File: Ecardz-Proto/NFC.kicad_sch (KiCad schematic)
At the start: 1 part, among them J1 Raspberry_Pi_2_3

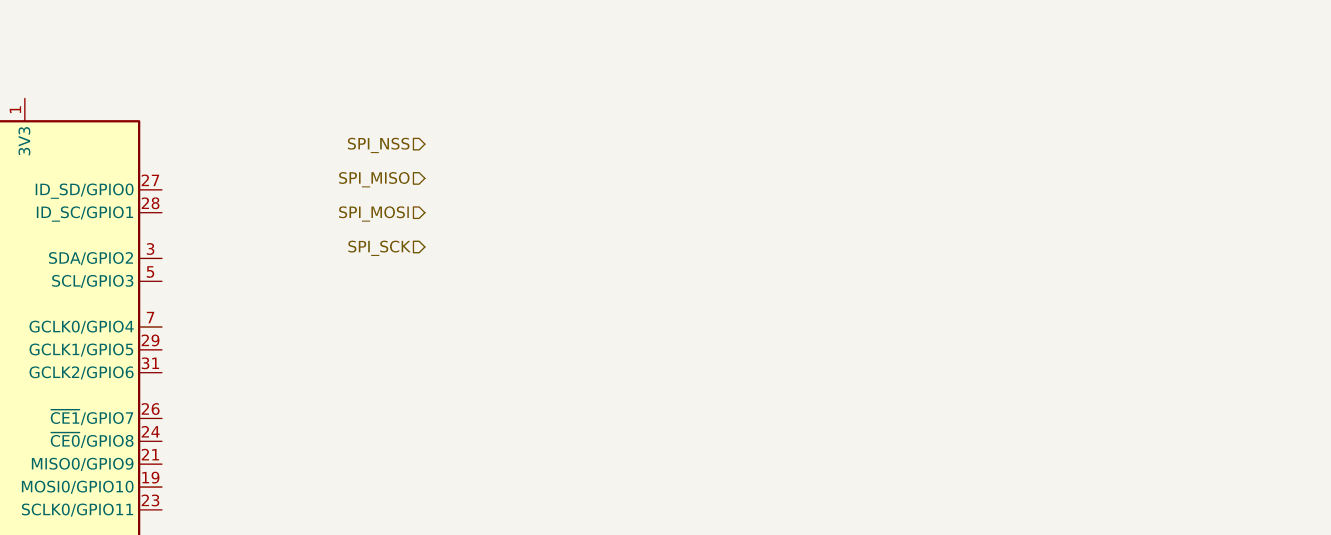
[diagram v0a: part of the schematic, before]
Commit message: added energy harvesting sensing ADC to NFC
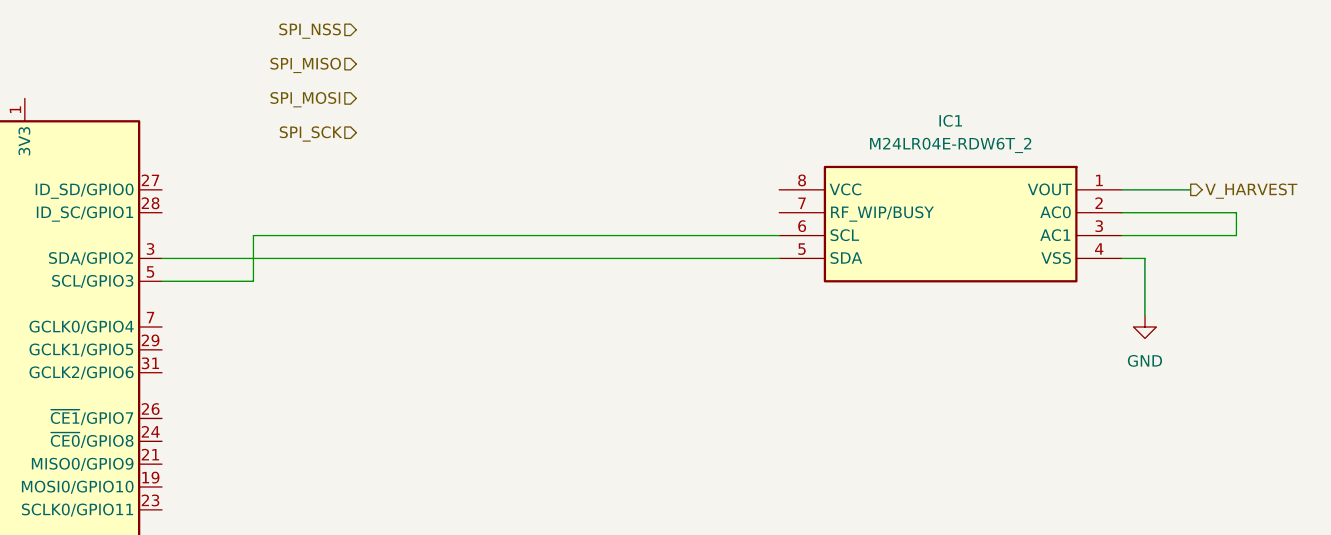
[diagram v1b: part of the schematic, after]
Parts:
- added IC1: M24LR04E-RDW6T_2, SOP65P640X120-8N, symbol SamacSys_Parts:M24LR04E-RDW6T_2
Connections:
- net at J1.3 (SDA/GPIO2): now also IC1.5 (SDA)
- net at J1.5 (SCL/GPIO3): now also IC1.6 (SCL)
- new net: IC1.2 (AC0), IC1.3 (AC1)
- new net GND: IC1.4 (VSS)
- new net V_HARVEST: IC1.1 (VOUT)

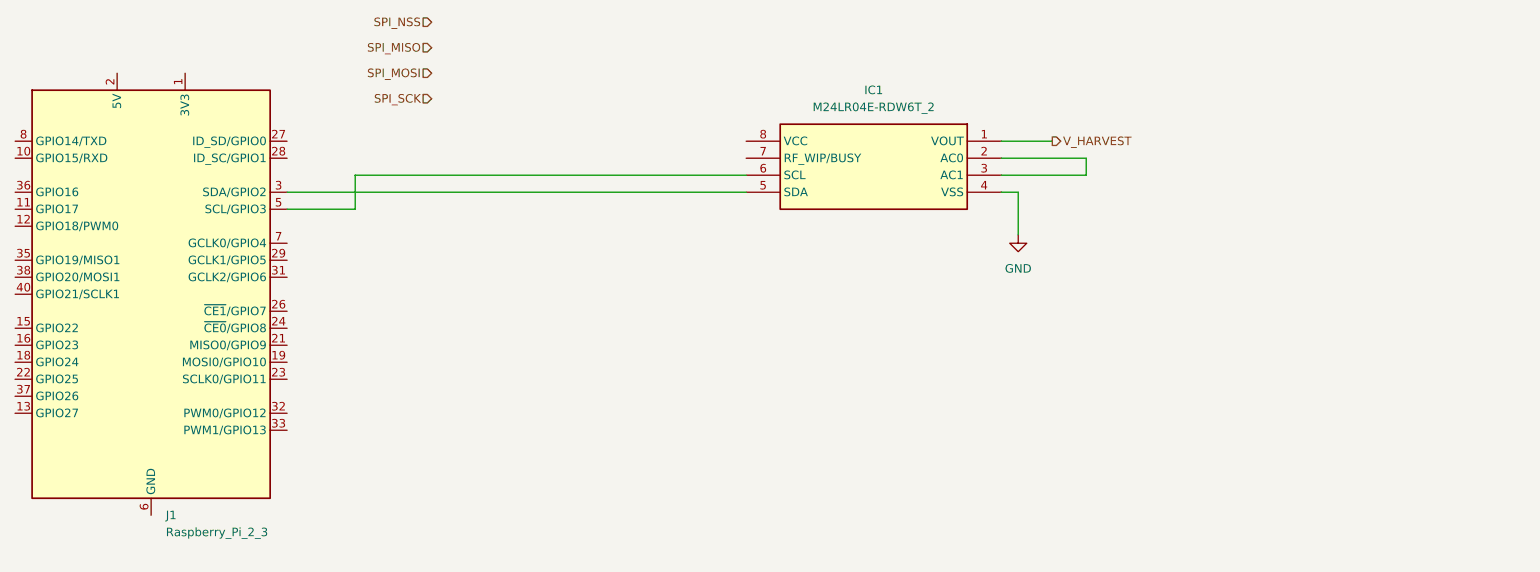
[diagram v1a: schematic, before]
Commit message: added STM and rpi pin connections.
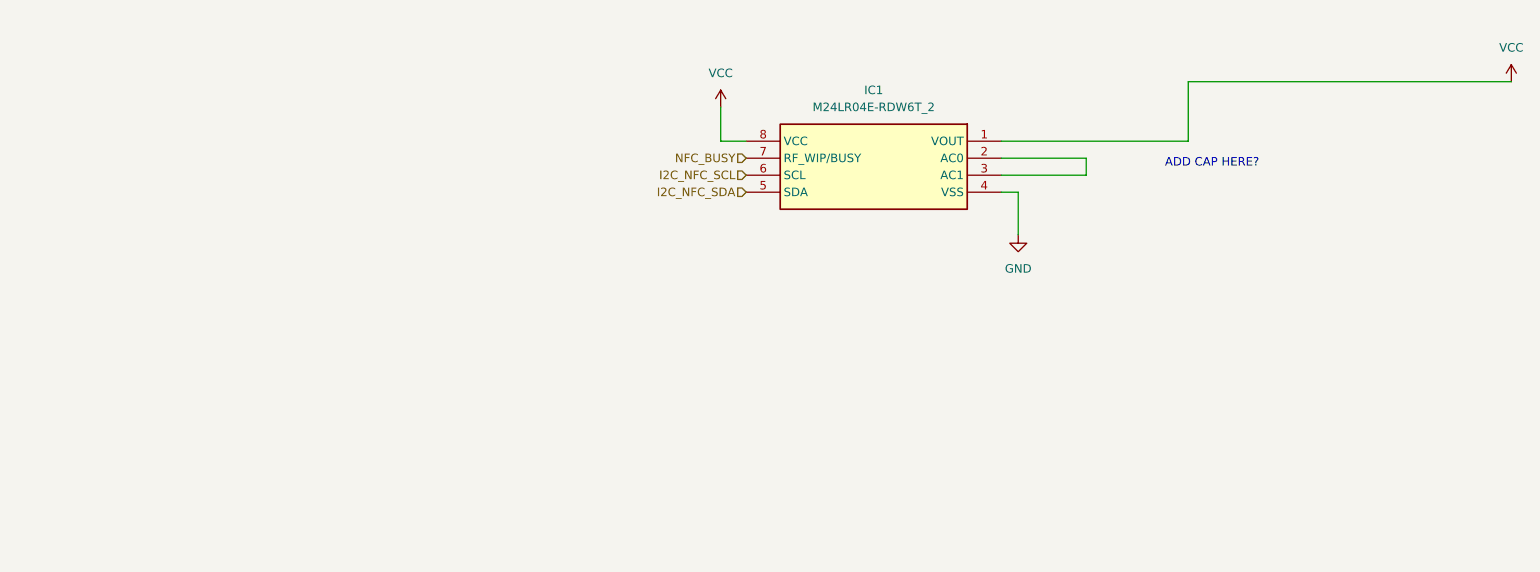
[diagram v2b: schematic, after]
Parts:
- removed J1: Raspberry_Pi_2_3, symbol Connector:Raspberry_Pi_2_3
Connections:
- net V_HARVEST is gone; now on net VCC: IC1.1 (VOUT)
- net I2C_NFC_SDA: now reaches IC1.5 (SDA)
- net I2C_NFC_SCL: now reaches IC1.6 (SCL)
- net NFC_BUSY: now reaches IC1.7 (RF_WIP/BUSY)
- net VCC: now reaches IC1.8 (VCC)
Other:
- note added: "ADD CAP HERE?"
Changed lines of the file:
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@@
 	(wire
 		(pts
-			(xy 81.28 39.37) (xy 81.28 44.45)
-		)
-		(stroke
-			(width 0)
-			(type default)
-		)
-	)
-	(wire
-		(pts
-			(xy 139.7 39.37) (xy 81.28 39.37)
+			(xy 135.89 34.29) (xy 139.7 34.29)
 		)
 		(stroke
@@
 	(wire
 		(pts
+			(xy 205.74 34.29) (xy 177.8 34.29)
+		)
+		(stroke
+			(width 0)
+			(type default)
+		)
+	)
+	(wire
+		(pts
 			(xy 177.8 36.83) (xy 190.5 36.83)
 		)
@@
 	(wire
 		(pts
-			(xy 177.8 34.29) (xy 185.42 34.29)
+			(xy 135.89 29.21) (xy 135.89 34.29)
+		)
+		(stroke
+			(width 0)
+			(type default)
+		)
+	)
+	(wire
+		(pts
+			(xy 205.74 25.4) (xy 254 25.4)
 		)
 		(stroke
@@
 	(wire
 		(pts
-			(xy 81.28 44.45) (xy 71.12 44.45)
-		)
-		(stroke
-			(width 0)
-			(type default)
-		)
-	)
-	(wire
-		(pts
 			(xy 180.34 48.26) (xy 180.34 41.91)
 		)
@@
 	(wire
 		(pts
-			(xy 71.12 41.91) (xy 139.7 41.91)
-		)
-		(stroke
-			(width 0)
-			(type default)
-		)
-	)
-	(hierarchical_label "SPI_MISO"
-		(shape input)
-		(at 92.71 20.32 180)
-		(fields_autoplaced yes)
+			(xy 205.74 25.4) (xy 205.74 34.29)
+		)
+		(stroke
+			(width 0)
+			(type default)
+		)
+	)
+	(text "ADD CAP HERE?\n"
+		(exclude_from_sim no)
+		(at 209.296 37.592 0)
 		(effects
 			(font
 				(size 1.27 1.27)
 			)
-			(justify right)
-		)
-	)
-	(hierarchical_label "SPI_MOSI"
+		)
+	)
+	(hierarchical_label "I2C_NFC_SDA"
 		(shape input)
-		(at 92.71 24.13 180)
+		(at 139.7 41.91 180)
 		(fields_autoplaced yes)
 		(effects
@@
 		)
 	)
-	(hierarchical_label "V_HARVEST"
-		(shape output)
-		(at 185.42 34.29 0)
+	(hierarchical_label "NFC_BUSY"
+		(shape input)
+		(at 139.7 36.83 180)
 		(fields_autoplaced yes)
 		(effects
@@
 				(size 1.27 1.27)
 			)
-			(justify left)
-		)
-	)
-	(hierarchical_label "SPI_SCK"
+			(justify right)
+		)
+	)
+	(hierarchical_label "I2C_NFC_SCL"
 		(shape input)
-		(at 92.71 27.94 180)
+		(at 139.7 39.37 180)
 		(fields_autoplaced yes)
 		(effects
@@
 		)
 	)
-	(hierarchical_label "SPI_NSS"
-		(shape input)
-		(at 92.71 16.51 180)
-		(fields_autoplaced yes)
-		(effects
-			(font
-				(size 1.27 1.27)
-			)
-			(justify right)
+	(symbol
+		(lib_id "power:VCC")
+		(at 135.89 29.21 0)
+		(unit 1)
+		(exclude_from_sim no)
+		(in_bom yes)
+		(on_board yes)
+		(dnp no)
+		(fields_autoplaced yes)
+		(property "Reference" "#PWR011"
+			(at 135.89 33.02 0)
+			(effects
+				(font
+					(size 1.27 1.27)
+				)
+				(hide yes)
+			)
+		)
+		(property "Value" "VCC"
+			(at 135.89 24.13 0)
+			(effects
+				(font
+					(size 1.27 1.27)
+				)
+			)
+		)
+		(property "Footprint" ""
+			(at 135.89 29.21 0)
+			(effects
+				(font
+					(size 1.27 1.27)
+				)
+				(hide yes)
+			)
+		)
+		(property "Datasheet" ""
+			(at 135.89 29.21 0)
+			(effects
+				(font
+					(size 1.27 1.27)
+				)
+				(hide yes)
+			)
+		)
+		(property "Description" "Power symbol creates a global label with name \"VCC\""
+			(at 135.89 29.21 0)
+			(effects
+				(font
+					(size 1.27 1.27)
+				)
+				(hide yes)
+			)
+		)
+		(pin "1"
+		)
+		(instances
+			(project "Ecardz-Proto"
+				(path "/2adbba85-9270-4efb-857d-656bb51406ca/95527a5c-8cb7-439d-944b-2d67c4df2ece"
+					(reference "#PWR011")
+					(unit 1)
+				)
+			)
 		)
 	)
@@
 		)
 		(instances
-			(project ""
+			(project "Ecardz-Proto"
 				(path "/2adbba85-9270-4efb-857d-656bb51406ca/95527a5c-8cb7-439d-944b-2d67c4df2ece"
 					(reference "IC1")
@@
 		)
 		(instances
-			(project ""
+			(project "Ecardz-Proto"
 				(path "/2adbba85-9270-4efb-857d-656bb51406ca/95527a5c-8cb7-439d-944b-2d67c4df2ece"
 					(reference "#PWR06")
@@
 	)
 	(symbol
-		(lib_id "Connector:Raspberry_Pi_2_3")
-		(at 50.8 57.15 0)
+		(lib_id "power:VCC")
+		(at 254 25.4 0)
 		(unit 1)
 		(exclude_from_sim no)
@@
 		(dnp no)
 		(fields_autoplaced yes)
-		(property "Reference" "J1"
-			(at 52.9941 90.17 0)
-			(effects
-				(font
-					(size 1.27 1.27)
-				)
-				(justify left)
-			)
-		)
-		(property "Value" "Raspberry_Pi_2_3"
-			(at 52.9941 92.71 0)
-			(effects
-				(font
-					(size 1.27 1.27)
-				)
-				(justify left)
+		(property "Reference" "#PWR010"
+			(at 254 29.21 0)
+			(effects
+				(font
+					(size 1.27 1.27)
+				)
+				(hide yes)
+			)
+		)
+		(property "Value" "VCC"
+			(at 254 20.32 0)
+			(effects
+				(font
+					(size 1.27 1.27)
+				)
 			)
 		)
 		(property "Footprint" ""
-			(at 50.8 57.15 0)
-			(effects
-				(font
-					(size 1.27 1.27)
-				)
-				(hide yes)
-			)
-		)
-		(property "Datasheet" "https://www.raspberrypi.org/documentation/hardware/raspberrypi/schematics/rpi_SCH_3bplus_1p0_reduced.pdf"
-			(at 111.76 101.6 0)
-			(effects
-				(font
-					(size 1.27 1.27)
-				)
-				(hide yes)
-			)
-		)
-		(property "Description" "expansion header for Raspberry Pi 2 & 3"
-			(at 50.8 57.15 0)
-			(effects
-				(font
-					(size 1.27 1.27)
-				)
-				(hide yes)
-			)
-		)
-		(pin "11"
-		)
-		(pin "19"
-		)
-		(pin "28"
-		)
-		(pin "30"
-		)
-		(pin "15"
-		)
-		(pin "20"
-		)
-		(pin "12"
-		)
-		(pin "17"
-		)
-		(pin "2"
-		)
-		(pin "25"
-		)
-		(pin "29"
-		)
-		(pin "13"
+			(at 254 25.4 0)
+			(effects
+				(font
+					(size 1.27 1.27)
+				)
+				(hide yes)
+			)
+		)
+		(property "Datasheet" ""
+			(at 254 25.4 0)
+			(effects
+				(font
+					(size 1.27 1.27)
+				)
+				(hide yes)
+			)
+		)
+		(property "Description" "Power symbol creates a global label with name \"VCC\""
+			(at 254 25.4 0)
+			(effects
+				(font
+					(size 1.27 1.27)
+				)
+				(hide yes)
+			)
 		)
 		(pin "1"
-		)
-		(pin "14"
-		)
-		(pin "16"
-		)
-		(pin "27"
-		)
-		(pin "33"
-		)
-		(pin "3"
-		)
-		(pin "26"
-		)
-		(pin "32"
-		)
-		(pin "36"
-		)
-		(pin "18"
-		)
-		(pin "24"
-		)
-		(pin "23"
-		)
-		(pin "39"
-		)
-		(pin "4"
-		)
-		(pin "40"
-		)
-		(pin "35"
-		)
-		(pin "6"
-		)
-		(pin "38"
-		)
-		(pin "7"
-		)
-		(pin "5"
-		)
-		(pin "37"
-		)
-		(pin "8"
-		)
-		(pin "9"
-		)
-		(pin "34"
-		)
-		(pin "21"
-		)
-		(pin "10"
-		)
-		(pin "31"
-		)
-		(pin "22"
 		)
 		(instances
 			(project "Ecardz-Proto"
 				(path "/2adbba85-9270-4efb-857d-656bb51406ca/95527a5c-8cb7-439d-944b-2d67c4df2ece"
-					(reference "J1")
+					(reference "#PWR010")
 					(unit 1)
 				)

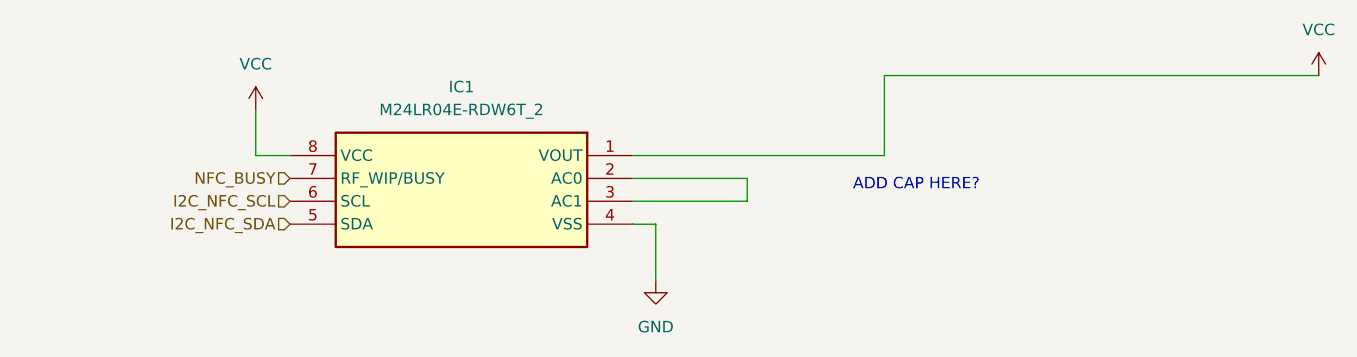
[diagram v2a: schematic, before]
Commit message: made all supply voltages VDD rather than mix of VDD/VCC, added VDD measurement via STM32 internal ADC, put DNP jumper for VPP on E-ink connector, and made NFC VCC pin only connected to power if externally powered
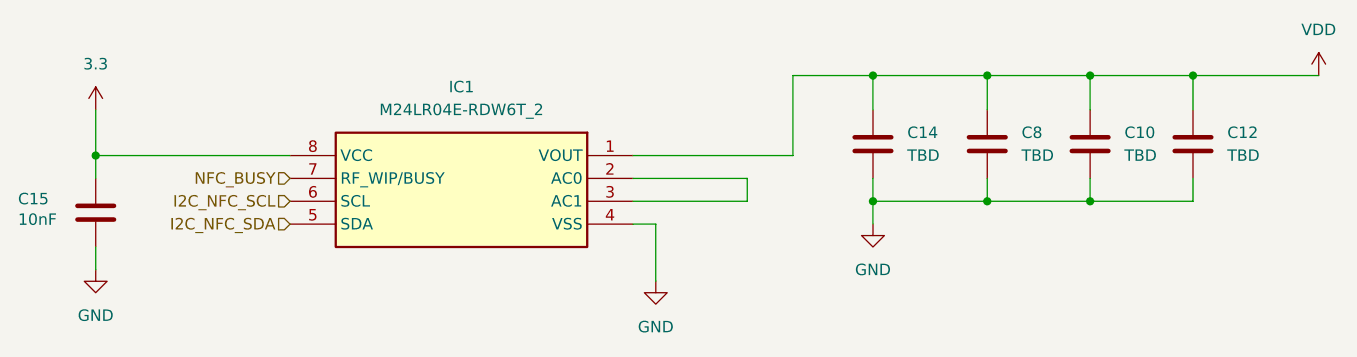
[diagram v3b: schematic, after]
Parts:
- added C10, C12, C14, C8: TBD, symbol Device:C
- added C15: 10nF, symbol Device:C
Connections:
- net GND: now also C10.2, C12.2, C14.2, C15.2, C8.2
- net VCC renamed 3.3
- net 3.3: now also C15.1; no longer IC1.1 (VOUT)
- new net VDD: C10.1, C12.1, C14.1, C8.1, IC1.1 (VOUT)
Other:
- note removed: "ADD CAP HERE?"

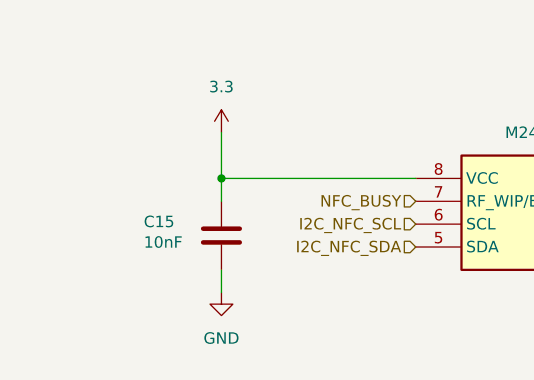
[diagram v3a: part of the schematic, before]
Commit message: added jumpers to select NFC chip's power supply connection
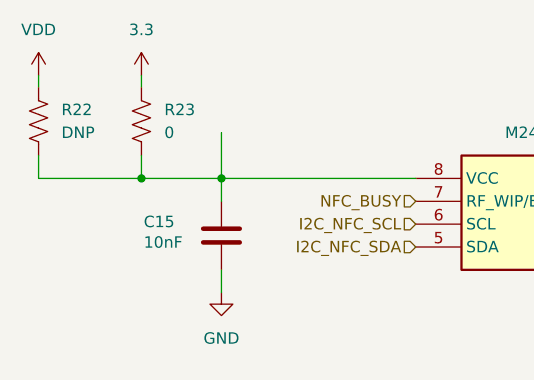
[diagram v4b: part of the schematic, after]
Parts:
- added R22: DNP, Resistor_SMD:R_0603_1608Metric_Pad0.98x0.95mm_HandSolder, symbol Device:R_US
- added R23: 0, Resistor_SMD:R_0603_1608Metric_Pad0.98x0.95mm_HandSolder, symbol Device:R_US
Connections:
- net 3.3: now also R23.2; no longer C15.1, IC1.8 (VCC)
- net VDD: now also R22.2
- new net: C15.1, IC1.8 (VCC), R22.1, R23.1

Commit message: updated most footprints
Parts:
- C10, C12, C14, C15, C8: footprint (none) -> Capacitor_SMD:C_0603_1608Metric_Pad1.08x0.95mm_HandSolder
- R23: value 0 -> DNP
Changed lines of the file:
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@@
 	(wire
 		(pts
-			(xy 118.11 29.21) (xy 118.11 34.29)
+			(xy 97.79 22.86) (xy 97.79 24.13)
 		)
 		(stroke
@@
 	(wire
 		(pts
-			(xy 97.79 22.86) (xy 97.79 24.13)
+			(xy 228.6 39.37) (xy 240.03 39.37)
 		)
 		(stroke
@@
 	(wire
 		(pts
-			(xy 228.6 39.37) (xy 240.03 39.37)
+			(xy 195.58 25.4) (xy 204.47 25.4)
 		)
 		(stroke
@@
 	(wire
 		(pts
-			(xy 195.58 25.4) (xy 204.47 25.4)
+			(xy 204.47 36.83) (xy 204.47 39.37)
 		)
 		(stroke
@@
 	(wire
 		(pts
-			(xy 204.47 36.83) (xy 204.47 39.37)
+			(xy 190.5 36.83) (xy 190.5 39.37)
 		)
 		(stroke
@@
 	(wire
 		(pts
-			(xy 190.5 36.83) (xy 190.5 39.37)
+			(xy 240.03 39.37) (xy 240.03 36.83)
 		)
 		(stroke
@@
 	(wire
 		(pts
-			(xy 240.03 39.37) (xy 240.03 36.83)
+			(xy 180.34 48.26) (xy 180.34 41.91)
 		)
 		(stroke
@@
 	(wire
 		(pts
-			(xy 180.34 48.26) (xy 180.34 41.91)
+			(xy 204.47 29.21) (xy 204.47 25.4)
 		)
 		(stroke
@@
 	(wire
 		(pts
-			(xy 204.47 29.21) (xy 204.47 25.4)
+			(xy 109.22 34.29) (xy 97.79 34.29)
 		)
 		(stroke
@@
 	(wire
 		(pts
-			(xy 109.22 34.29) (xy 97.79 34.29)
+			(xy 195.58 25.4) (xy 195.58 34.29)
 		)
 		(stroke
@@
 	(wire
 		(pts
-			(xy 195.58 25.4) (xy 195.58 34.29)
+			(xy 240.03 25.4) (xy 254 25.4)
 		)
 		(stroke
@@
 		)
 	)
-	(wire
-		(pts
-			(xy 240.03 25.4) (xy 254 25.4)
-		)
-		(stroke
-			(width 0)
-			(type default)
-		)
-	)
 	(hierarchical_label "I2C_NFC_SDA"
 		(shape input)
@@
 			)
 		)
-		(property "Footprint" ""
+		(property "Footprint" "Capacitor_SMD:C_0603_1608Metric_Pad1.08x0.95mm_HandSolder"
 			(at 240.9952 36.83 0)
 			(effects
@@
 			)
 		)
-		(property "Footprint" ""
+		(property "Footprint" "Capacitor_SMD:C_0603_1608Metric_Pad1.08x0.95mm_HandSolder"
 			(at 119.0752 44.45 0)
 			(effects
@@
 			)
 		)
-		(property "Footprint" ""
+		(property "Footprint" "Capacitor_SMD:C_0603_1608Metric_Pad1.08x0.95mm_HandSolder"
 			(at 218.1352 36.83 0)
 			(effects
@@
 		)
 		(instances
-			(project ""
+			(project "Ecardz-Proto"
 				(path "/2adbba85-9270-4efb-857d-656bb51406ca/95527a5c-8cb7-439d-944b-2d67c4df2ece"
 					(reference "C8")
@@
 			)
 		)
-		(property "Footprint" ""
+		(property "Footprint" "Capacitor_SMD:C_0603_1608Metric_Pad1.08x0.95mm_HandSolder"
 			(at 205.4352 36.83 0)
 			(effects
@@
 			)
 		)
-		(property "Value" "0"
+		(property "Value" "DNP"
 			(at 111.76 29.2099 0)
 			(effects
@@
 			)
 		)
-		(property "Footprint" ""
+		(property "Footprint" "Capacitor_SMD:C_0603_1608Metric_Pad1.08x0.95mm_HandSolder"
 			(at 229.5652 36.83 0)
 			(effects

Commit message: added a C_2917 cap to NFC energy harvesting in case needed
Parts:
- C14: footprint Capacitor_SMD:C_0603_1608Metric_Pad1.08x0.95mm_HandSolder -> parts-lib:C_2917
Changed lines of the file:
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@@
 			)
 		)
-		(property "Footprint" "Capacitor_SMD:C_0603_1608Metric_Pad1.08x0.95mm_HandSolder"
+		(property "Footprint" "parts-lib:C_2917"
 			(at 205.4352 36.83 0)
 			(effects
